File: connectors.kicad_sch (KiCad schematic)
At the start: 25 parts, among them J10 Conn_01x03, J11 Conn_01x03, J5 Conn_01x02_Socket, J6 Conn_01x02_Socket, J7 Conn_01x02_Socket, J8 Conn_01x03, J9 Conn_01x05, Q10 DMG3420U, Q8 DMG3420U, Q9 DMP2305U

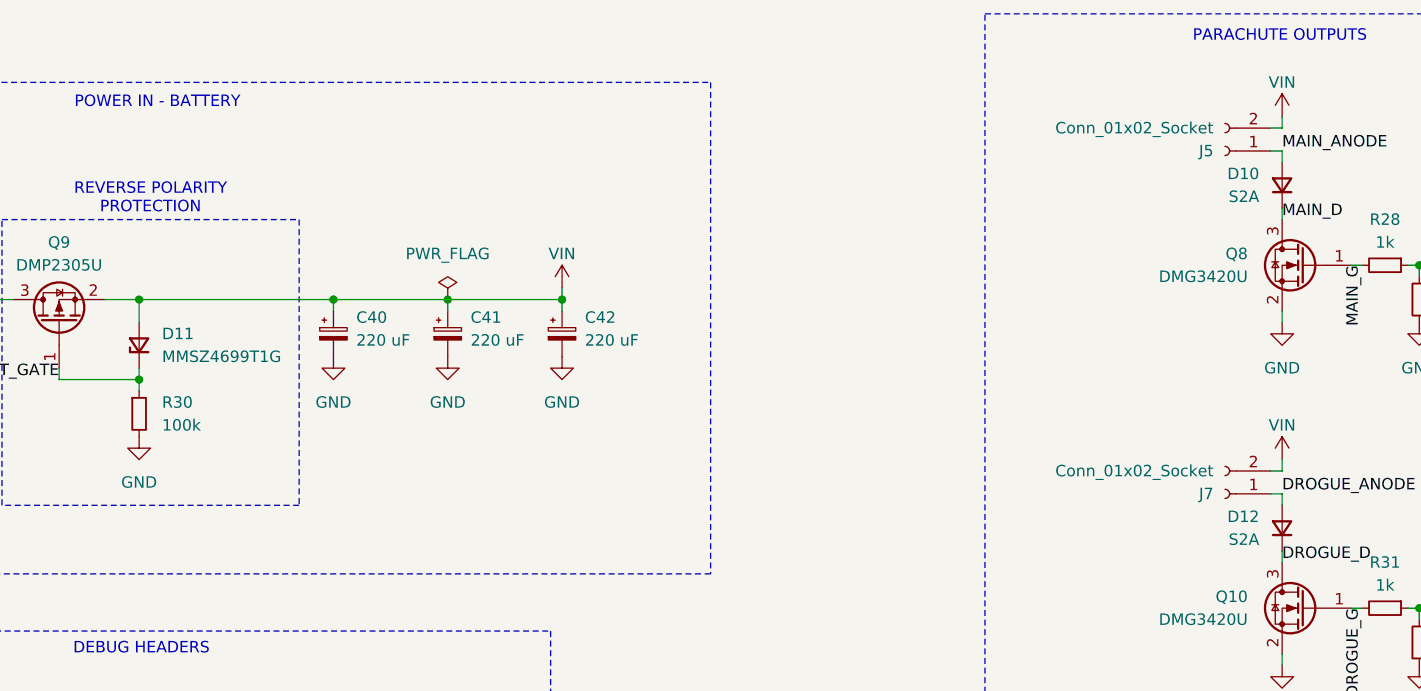
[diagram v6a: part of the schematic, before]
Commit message: Added more graphics, removed some unnecessary features. moved GPU passive components upper. added switching components to LoRa.
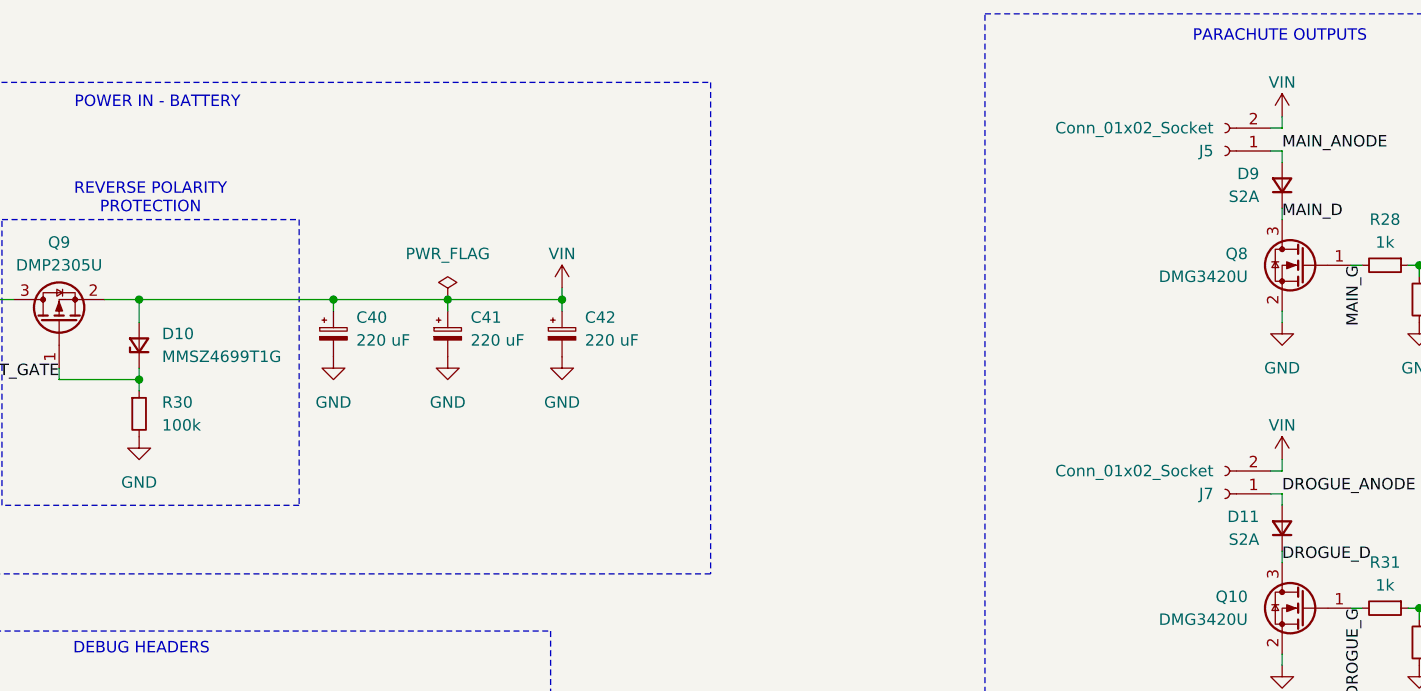
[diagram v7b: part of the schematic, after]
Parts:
- renumbered D11 to D10, D12 to D11, D10 to D9
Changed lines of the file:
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@@
 		(on_board yes)
 		(dnp no)
-		(property "Reference" "D10"
+		(property "Reference" "D9"
 			(at 215.9 54.6099 90)
 			(effects
@@
 			(project ""
 				(path "/d24fd15c-a242-4d26-9876-7755ca0d378c/6620a15d-5243-4c14-a303-2b39928e4e3b"
-					(reference "D10")
+					(reference "D9")
 					(unit 1)
 				)
@@
 		(on_board yes)
 		(dnp no)
-		(property "Reference" "D12"
+		(property "Reference" "D11"
 			(at 215.9 92.7099 90)
 			(effects
@@
 			(project "valkyriev3"
 				(path "/d24fd15c-a242-4d26-9876-7755ca0d378c/6620a15d-5243-4c14-a303-2b39928e4e3b"
-					(reference "D12")
+					(reference "D11")
 					(unit 1)
 				)
@@
 		(dnp no)
 		(fields_autoplaced yes)
-		(property "Reference" "D11"
+		(property "Reference" "D10"
 			(at 93.98 72.3899 90)
 			(effects
@@
 			(project ""
 				(path "/d24fd15c-a242-4d26-9876-7755ca0d378c/6620a15d-5243-4c14-a303-2b39928e4e3b"
-					(reference "D11")
-					(unit 1)
-				)
+					(reference "D10")
+					(unit 1)
+				)
